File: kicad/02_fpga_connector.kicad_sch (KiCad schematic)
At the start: 0 parts

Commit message: Phase 1: sheet 2 (fpga connector) transcribed; sheet scripts, renderer, pending-split warnings
Co-Authored-By: Claude Fable 5.1 <noreply@anthropic.com>
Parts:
- added J1, J2, J3, J4, J6, J8: HB GT CONNECTOR, symbol ac_psu:HB_GT_CONNECTOR
- added J11: 38 PIN HEADER 50TH, symbol ac_psu:HEADER_38_50MIL
- added J12: 2X3 PIN 50TH CONNECTOR, symbol ac_psu:HEADER_2X3_43_48
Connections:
- new net 20V: J1.48, J2.48, J3.48
- new net 20V_ISO_SEC: J4.48, J6.48, J8.48
- new net 5V: J1.45, J2.45, J3.45
- new net 5V_ISOL: J12.44, J12.46, J12.48, J4.45, J6.45, J8.45
- new net ADASEL0_ISO: J11.11
- new net ADASEL1_ISO: J11.10
- new net ADASEL2_ISO: J11.9
- new net ADCLK_DAB: J11.24
- new net ADCLK_ISO: J11.7
- new net CLK1_ISO: J11.14
- new net CS1_ISO: J11.13
- new net DAB_GATE_HI_PRI: J3.21, J3.22, J3.23, J3.24, J3.26
- new net DAB_GATE_HI_SEC: J4.35, J4.36, J4.37, J4.38, J4.40
- new net DAB_GATE_LO_PRI: J3.35, J3.36, J3.37, J3.38, J3.40
- new net DAB_GATE_LO_SEC: J4.21, J4.22, J4.23, J4.24, J4.26
- new net DAB_PWM_HI_SEC: J11.27, J4.43
- new net DAB_PWM_LO_SEC: J11.29, J4.44
- new net DAB_PWM_PRI_HI: J3.43
- new net DAB_PWM_PRI_HI_ISO: J11.22
- new net DAB_PWM_PRI_LO: J3.44
- new net DAB_PWM_PRI_LO_ISO: J11.23
- new net DAB_SOURCE_HI_PRI: J3.15, J3.16, J3.17, J3.18, J3.19, J3.20
- new net DAB_SOURCE_HI_SEC: J4.29, J4.30, J4.31, J4.32, J4.33, J4.34
- new net DAB_SOURCE_LO_PRI: J3.29, J3.30, J3.31, J3.32, J3.33, J3.34
- new net DAB_SOURCE_LO_SEC: J4.15, J4.16, J4.17, J4.18, J4.19, J4.20
- new net G1_GATE_HI: J2.35, J2.36, J2.37, J2.38, J2.40
- new net G1_SOURCE_HI: J2.29, J2.30, J2.31, J2.32, J2.33, J2.34
- new net G2_GATE_LO: J1.21, J1.22, J1.23, J1.24, J1.26
- new net G2_SOURCE_LO: J1.15, J1.16, J1.17, J1.18, J1.19, J1.20
- new net G3_GATE_HI: J2.21, J2.22, J2.23, J2.24, J2.26
- new net G3_SOURCE_HI: J2.15, J2.16, J2.17, J2.18, J2.19, J2.20
- new net G4_GATE_LO: J1.35, J1.36, J1.37, J1.38, J1.40
- new net G4_SOURCE_LO: J1.29, J1.30, J1.31, J1.32, J1.33, J1.34
- new net GND: J1.46, J2.46, J3.46
- new net GPIO_BYPASS_RLY_ISO: J11.36
- new net GPIO_BYPASS_RLY_ISOLATED: J11.8
- new net INU_ADCLK: J11.32
- new net ISOADA1: J11.4
- new net ISOADA2: J11.3
- new net ISOADA3: J11.1
- new net ISOGND: J11.2, J11.5, J12.43, J12.45, J12.47, J4.46, J6.46, J8.46
- new net ISO_AFE_SDM_RAW_VOLTAGE: J8.39
- new net ISO_DAB_SDM_RAW_VOLTAGE: J4.25
- new net MDATA_DAB: J11.26
- new net MDATA_INU: J11.34
- new net MDATA_ISO: J11.6
- new net PWM_G1: J2.43
- new net PWM_G1_ISO: J11.20
- new net PWM_G2: J1.44
- new net PWM_G2_ISO: J11.19
- new net PWM_G3: J2.44
- new net PWM_G3_ISO: J11.21
- new net PWM_G4: J1.43
- new net PWM_G4_ISO: J11.18
- new net PWM_Q5: J11.30, J8.44
- new net PWM_Q6: J11.31, J6.43
- new net PWM_Q7: J11.37, J8.43
- new net PWM_Q8: J11.33, J6.44
- new net PWM_TRANS1: J1.47
- new net PWM_TRANS1_ISO: J11.15
- new net PWM_TRANS2: J2.47
- new net PWM_TRANS2_ISO: J11.16
- new net PWM_TRANS3: J3.47
- new net PWM_TRANS3_ISO: J11.17
- new net PWM_TRANS4: J11.25, J4.47
- new net PWM_TRANS5: J11.35, J6.47
- new net PWM_TRANS6: J11.28, J8.47
- new net Q5_G: J8.21, J8.22, J8.23, J8.24, J8.26
- new net Q5_S: J8.15, J8.16, J8.17, J8.18, J8.19, J8.20
- new net Q6_G: J6.35, J6.36, J6.37, J6.38, J6.40
- new net Q6_S: J6.29, J6.30, J6.31, J6.32, J6.33, J6.34
- new net Q7_G: J8.35, J8.36, J8.37, J8.38, J8.40
- new net Q7_S: J8.29, J8.30, J8.31, J8.32, J8.33, J8.34
- new net Q8_G: J6.21, J6.22, J6.23, J6.24, J6.26
- new net Q8_S: J6.15, J6.16, J6.17, J6.18, J6.19, J6.20
- new net SDATA1_ISO: J11.12
- new net SDM_RAW_VOLTAGE: J2.39
- no-connect marks 0 -> 10
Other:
- note added: "PWR_FLAGs for the supplies entering through the connectors (temporary, see STATUS.md)"

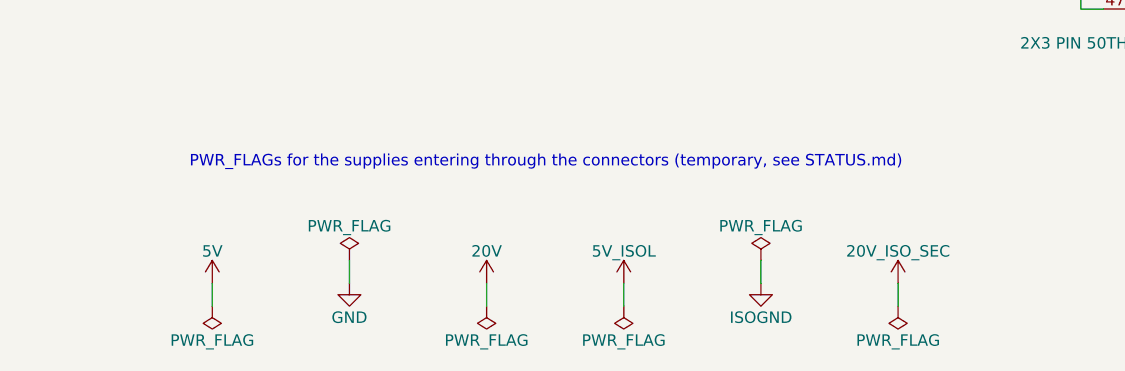
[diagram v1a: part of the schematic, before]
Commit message: Phase 1: sheet 3 (regulators) transcribed; centred field text for two-pin parts
Co-Authored-By: Claude Fable 5.1 <noreply@anthropic.com>
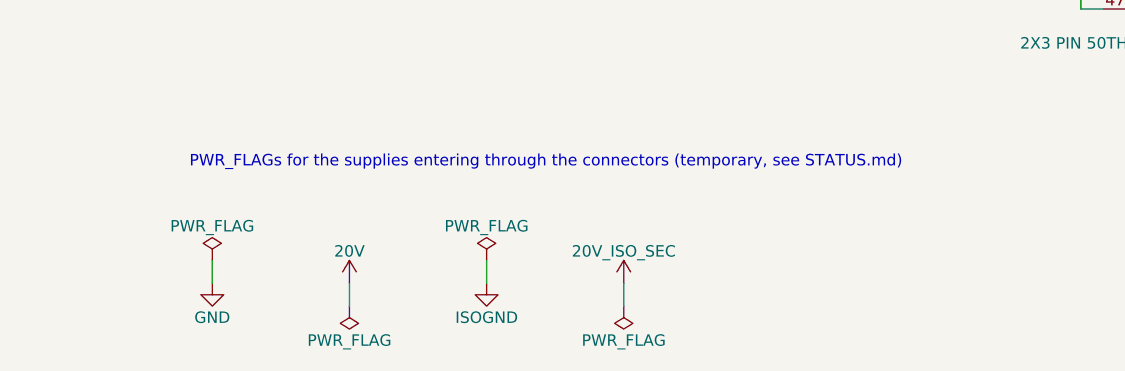
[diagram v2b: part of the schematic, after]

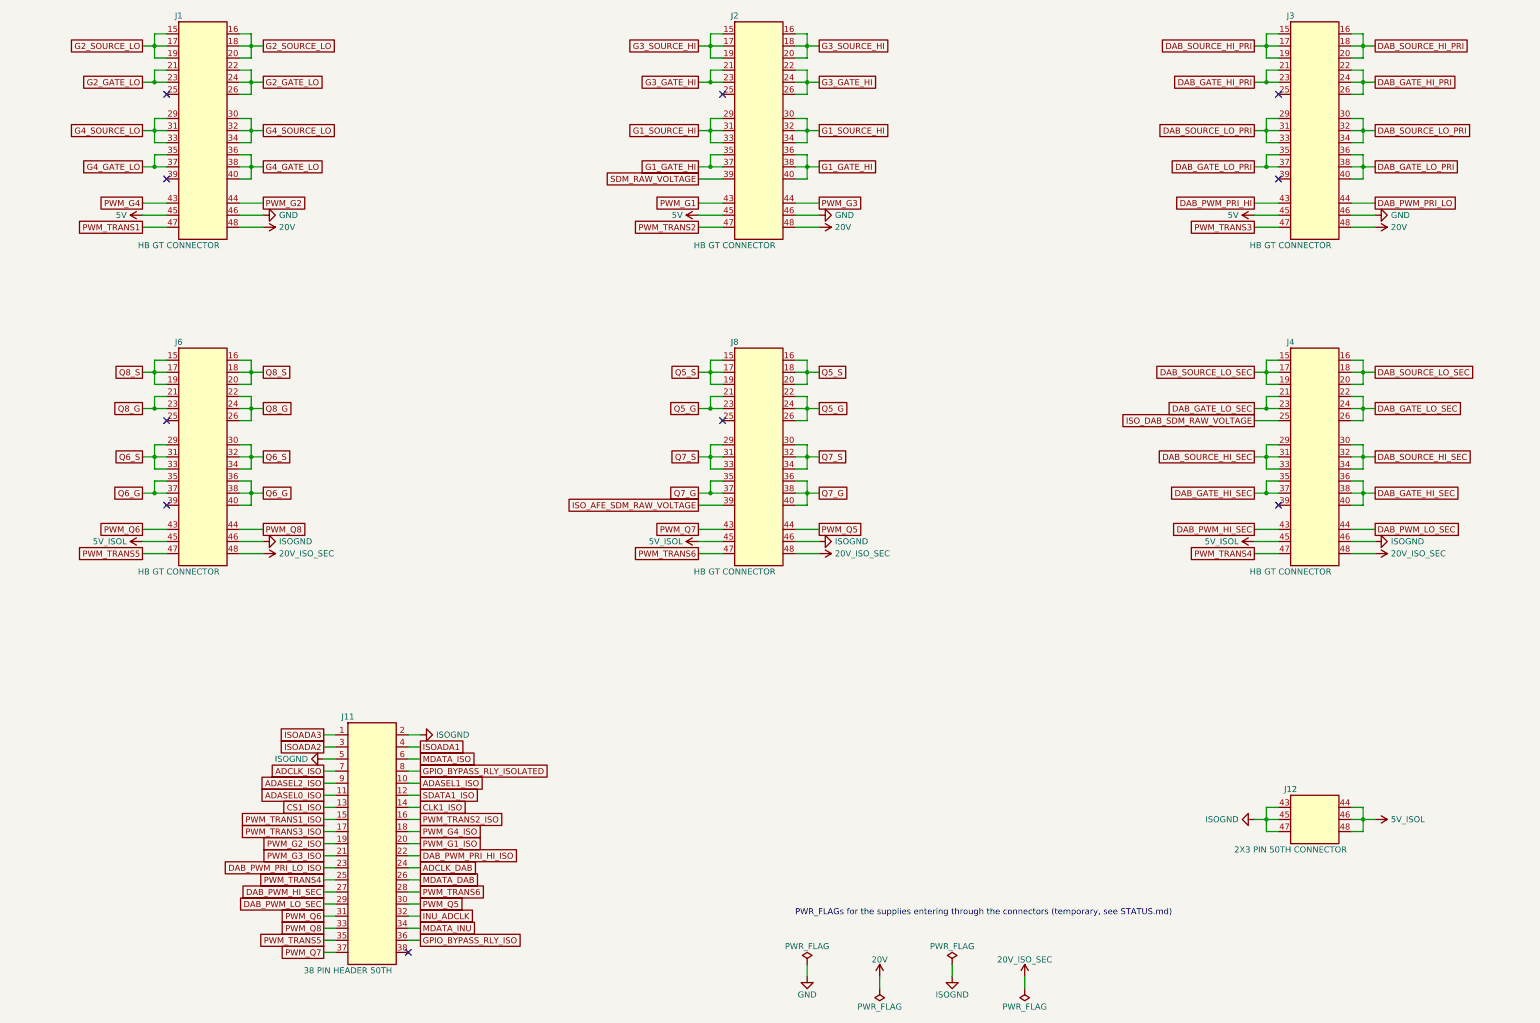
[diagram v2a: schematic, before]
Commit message: Phase 1: sheet 1 (afe); power symbols for PGND/ISOPGND/DAB_GROUND groups on sheet 2
Co-Authored-By: Claude Fable 5.1 <noreply@anthropic.com>
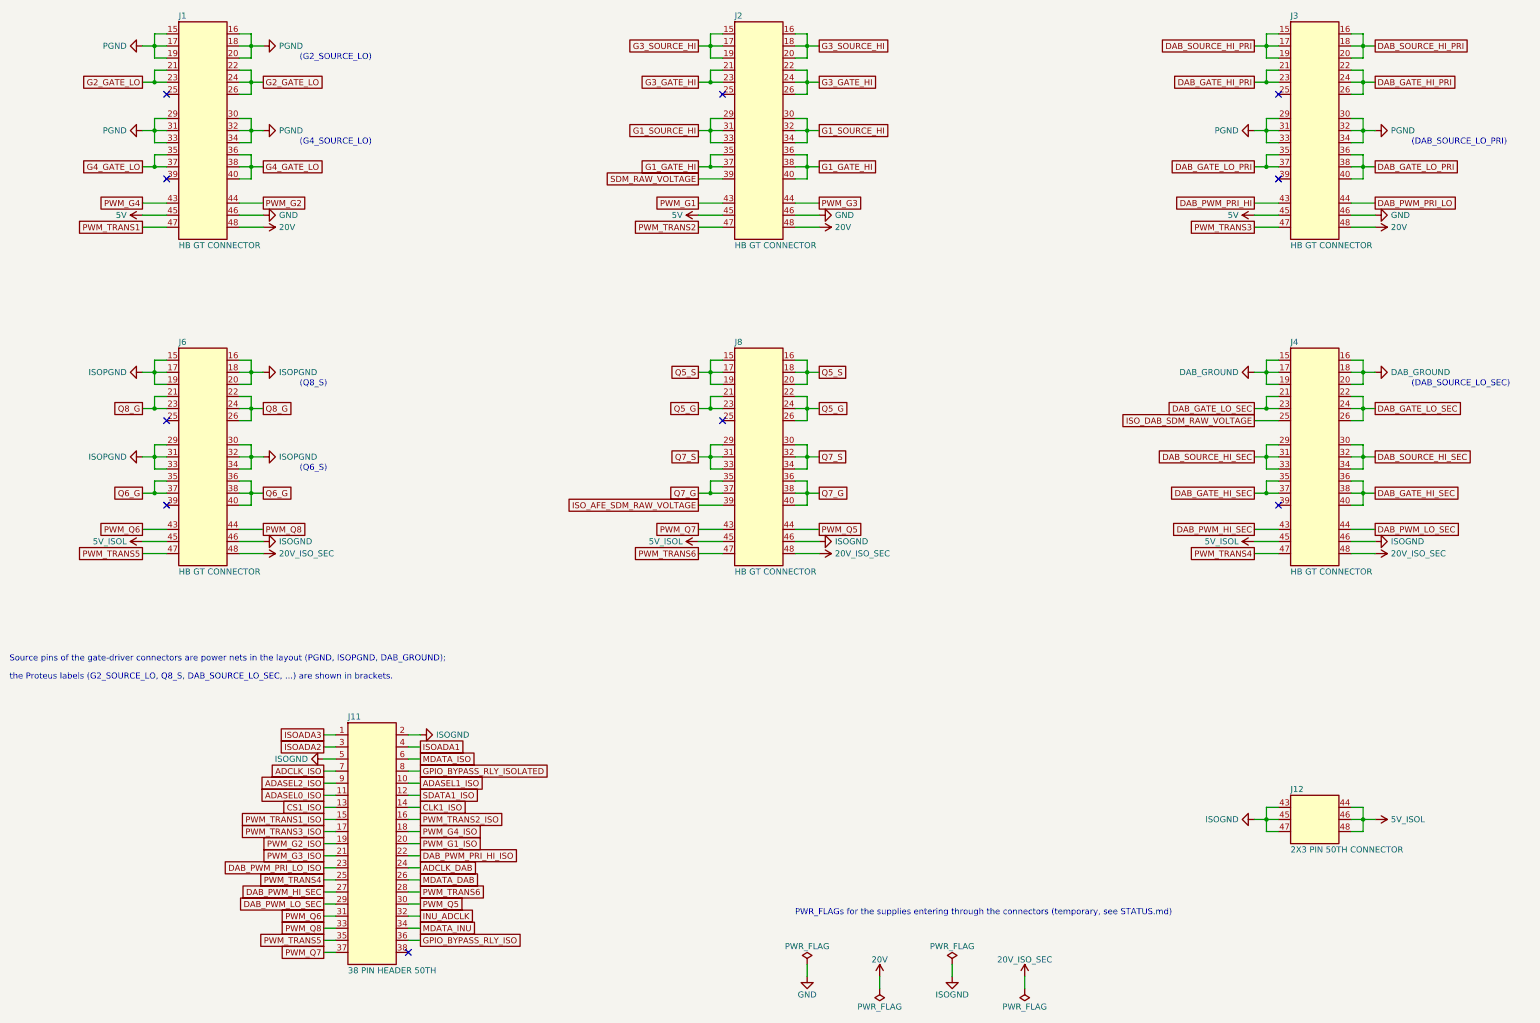
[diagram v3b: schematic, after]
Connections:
- net G2_SOURCE_LO is gone; now on net PGND: J1.15, J1.16, J1.17, J1.18, J1.19, J1.20
- net G4_SOURCE_LO is gone; now on net PGND: J1.29, J1.30, J1.31, J1.32, J1.33, J1.34
- net Q8_S is gone; now on net ISOPGND: J6.15, J6.16, J6.17, J6.18, J6.19, J6.20
- net DAB_SOURCE_LO_PRI renamed PGND
- net DAB_SOURCE_LO_SEC renamed DAB_GROUND
- net Q6_S renamed ISOPGND
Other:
- note added: "(DAB_SOURCE_LO_PRI)"
- note added: "(DAB_SOURCE_LO_SEC)"
- note added: "(G2_SOURCE_LO)"
- note added: "(G4_SOURCE_LO)"
- note added: "(Q6_S)"
- note added: "(Q8_S)"
- note added: "Source pins of the gate-driver connectors are power nets in the layout (PGND, ISOPGND, DAB_GROUND);"
- note added: "the Proteus labels (G2_SOURCE_LO, Q8_S, DAB_SOURCE_LO_SEC, ...) are shown in brackets."

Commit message: Phase 1 done: sheet 7 (aux supply), strict check_all, STATUS and Phase 2 handoff prompt
Co-Authored-By: Claude Fable 5.1 <noreply@anthropic.com>
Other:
- note added: "ISOGND enters the board through J12 / J4 / J6 / J8 (PWR_FLAG here); GND, 20V, 20V_ISO_SEC are flagged on sheet 7."
- note removed: "PWR_FLAGs for the supplies entering through the connectors (temporary, see STATUS.md)"

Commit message: Phase 2 done: footprints assigned and verified against IPC pads
- tools/gen_footprints.py -> lib/footprint_map.csv + lib/ac_psu.pretty (20 project footprints)
- tools/fpgeom.py: footprint pad loader and rigid fit; tools/check_footprints.py (+ pcbnew
  placement check), added to check_all.sh; reports/footprint_fit.csv for Phase 3 placement
- sch_builder: Footprint field from the map, deterministic UUIDs; all sheets regenerated
- kicad/fp-lib-table; STATUS.md (decisions, residuals, REF3025/C67 findings); Phase 3 prompt

Co-Authored-By: Claude Opus 5.5 <noreply@anthropic.com>
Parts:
- J1, J2, J3, J4, J6, J8: footprint (none) -> ac_psu:PinHeader_2x24_P1.27mm_Vertical_Pins15-48
- J11: footprint (none) -> Connector_PinHeader_1.27mm:PinHeader_2x19_P1.27mm_Vertical
- J12: footprint (none) -> ac_psu:PinHeader_2x03_P1.27mm_Vertical_Pins43-48
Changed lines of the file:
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@@
 			)
 		)
-		(property "Footprint" ""
+		(property "Footprint" "ac_psu:PinHeader_2x24_P1.27mm_Vertical_Pins15-48"
 			(at 66.04 53.34 0)
 			(effects
@@
 			)
 		)
-		(property "Footprint" ""
+		(property "Footprint" "ac_psu:PinHeader_2x24_P1.27mm_Vertical_Pins15-48"
 			(at 182.88 53.34 0)
 			(effects
@@
 			)
 		)
-		(property "Footprint" ""
+		(property "Footprint" "ac_psu:PinHeader_2x24_P1.27mm_Vertical_Pins15-48"
 			(at 299.72 53.34 0)
 			(effects
@@
 			)
 		)
-		(property "Footprint" ""
+		(property "Footprint" "ac_psu:PinHeader_2x24_P1.27mm_Vertical_Pins15-48"
 			(at 66.04 121.92 0)
 			(effects
@@
 			)
 		)
-		(property "Footprint" ""
+		(property "Footprint" "ac_psu:PinHeader_2x24_P1.27mm_Vertical_Pins15-48"
 			(at 182.88 121.92 0)
 			(effects
@@
 			)
 		)
-		(property "Footprint" ""
+		(property "Footprint" "ac_psu:PinHeader_2x24_P1.27mm_Vertical_Pins15-48"
 			(at 299.72 121.92 0)
 			(effects
@@
 			)
 		)
-		(property "Footprint" ""
+		(property "Footprint" "Connector_PinHeader_1.27mm:PinHeader_2x19_P1.27mm_Vertical"
 			(at 101.6 203.2 0)
 			(effects
@@
 			)
 		)
-		(property "Footprint" ""
+		(property "Footprint" "ac_psu:PinHeader_2x03_P1.27mm_Vertical_Pins43-48"
 			(at 299.72 198.12 0)
 			(effects

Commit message: Phase 3 done: PCB rebuilt from the Proteus gerbers with nets and zones
tools/make_pcb.sh regenerates kicad/ac_psu.kicad_pcb (byte-reproducible):
build_pcb.py (footprints with nets and symbol links at the Proteus
positions, outline, mounting holes, rules), gerber_to_tracks.py (4052
tracks, 173 vias; pour edge strokes recognised and skipped),
assign_nets.py (union-find over copper, 0 shorts/orphans/opens with
pours), pours_to_zones.py (79 zones = Proteus pour copper incl. holes).

New checks in check_all.sh: check_board.py (pads/holes/vias vs IPC),
assign_nets.py --check (after zone fill), drc.py (0 shorts, 0
unconnected, 0 parity issues; courtyard overlaps accepted).

Footprints (user decision): Proteus pad sizes for the headers, TSSOP,
SOT-23(-5), SOIC-16W packages whose KiCad pads shorted/violated
clearance; Proteus pads and drills for TO-247, VXO7805, P27.5 film and
snap-in caps; tighter courtyards for IPC-built footprints.

Co-Authored-By: Claude Opus 5.5 <noreply@anthropic.com>
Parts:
- J11: footprint Connector_PinHeader_1.27mm:PinHeader_2x19_P1.27mm_Vertical -> ac_psu:PinHeader_2x19_P1.27mm_Vertical_Proteus
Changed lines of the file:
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@@
 			)
 		)
-		(property "Footprint" "Connector_PinHeader_1.27mm:PinHeader_2x19_P1.27mm_Vertical"
+		(property "Footprint" "ac_psu:PinHeader_2x19_P1.27mm_Vertical_Proteus"
 			(at 101.6 203.2 0)
 			(effects
